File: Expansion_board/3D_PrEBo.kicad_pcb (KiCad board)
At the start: 2 copper layers, 100 x 84 mm, 74 parts, among them J1 LED, J10 TMC_INPUT, J11 Power_out, J12 Z_Probe, J13 Fan_interconnection_header, J14 X_MIN, J15 Z_MAX, J2 V_IN, J3 RJ45, J4 X, J5 Y, J6 Z, J7 E0, J8 E1, J9 FAN&LED_INPUT, M1 Fan_3pin, M2 Fan_3pin, M3 Fan_3pin, M4 Fan_3pin, M5 Fan_3pin, M6 Fan_3pin, M7 Fan_3pin, M8 Fan_4pin, Q1 AOD4189, Q10 IRLML2502, Q2 IRLML2502, Q3 IRLML2502, Q4 IRLML2502, Q5 IRLML2502, Q6 IRLML2502, Q7 IRLML2502, Q8 IRLML2502, Q9 IRLML2502, U1 L5973D, U2 NCP1117-5.0_SOT223

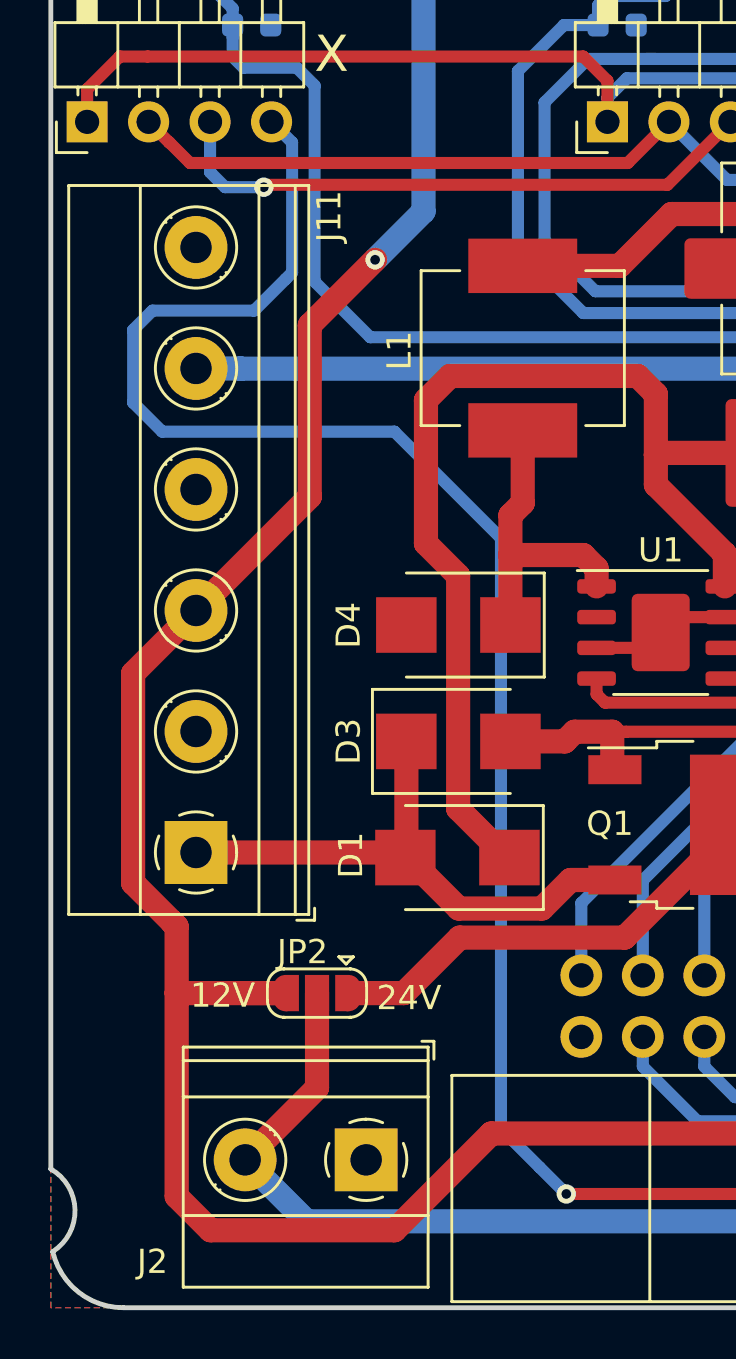
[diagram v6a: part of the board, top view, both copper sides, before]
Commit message: Expansion_board: PCB: Updated silkscreen for power connectors
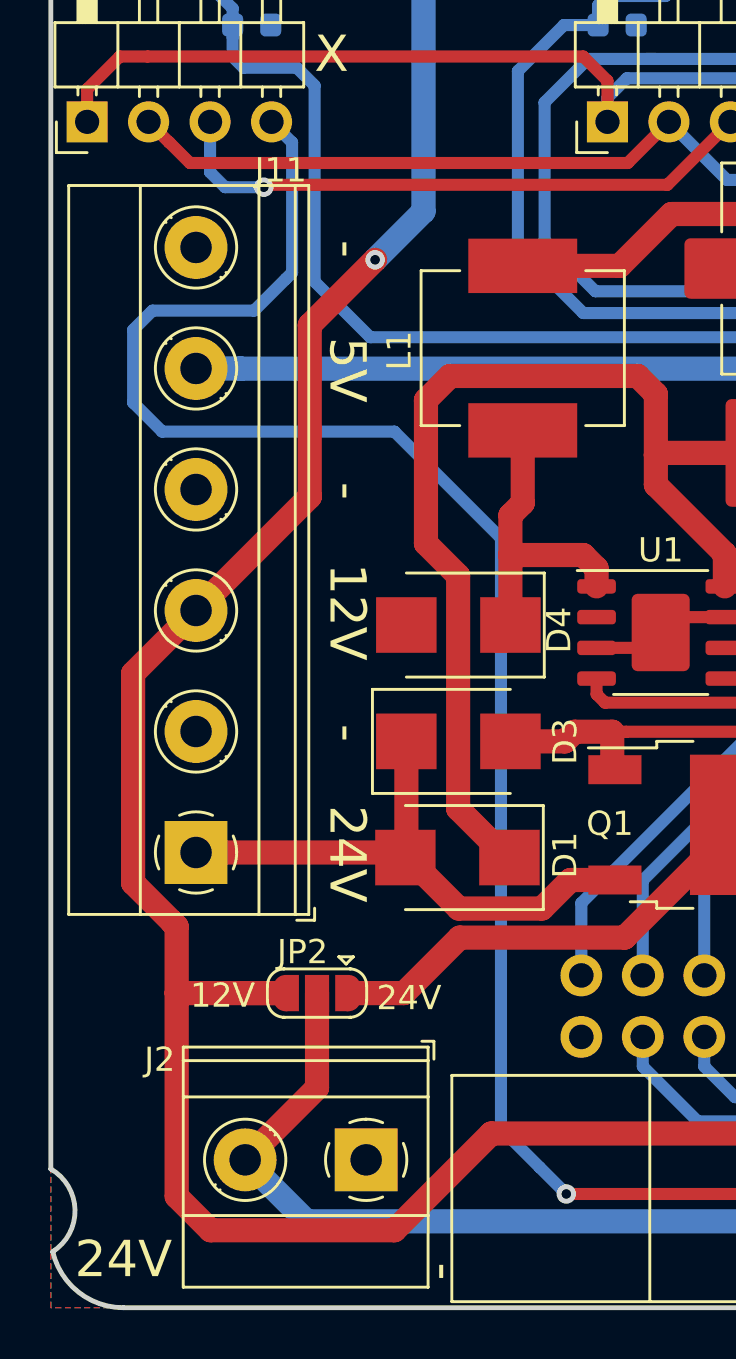
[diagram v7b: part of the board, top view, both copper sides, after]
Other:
- board text added: "-"
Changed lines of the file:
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@@
   (general
     (thickness 1.6)
-    (drawings 173)
+    (drawings 181)
     (tracks 683)
     (zones 0)
@@
     (visible_elements FFFFFFFF)
     (pcbplotparams
-      (layerselection 0x010fc_ffffffff)
-      (usegerberextensions false)
+      (layerselection 0x010f0_ffffffff)
+      (usegerberextensions true)
       (usegerberattributes false)
       (usegerberadvancedattributes false)
       (creategerberjobfile false)
-      (excludeedgelayer true)
+      (excludeedgelayer false)
       (linewidth 0.150000)
       (plotframeref false)
@@
       (outputformat 1)
       (mirror false)
-      (drillshape 1)
+      (drillshape 0)
       (scaleselection 1)
-      (outputdirectory ""))
+      (outputdirectory "gerbers/"))
   )
   (net 0 "")
@@
     (tags "Diode SMB (DO-214AA)")
     (attr smd)
-    (fp_text reference D1 (at 4.4 0.1 270) (layer F.SilkS)
+    (fp_text reference D1 (at -4.45 0.1 270) (layer F.SilkS)
       (effects (font (size 1 1) (thickness 0.15)))
     )
@@
     (tags "Diode SMB (DO-214AA)")
     (attr smd)
-    (fp_text reference D3 (at -4.54 0 90) (layer F.SilkS)
+    (fp_text reference D3 (at 4.41 0 90) (layer F.SilkS)
       (effects (font (size 1 1) (thickness 0.15)))
     )
@@
     (tags "Diode SMB (DO-214AA)")
     (attr smd)
-    (fp_text reference D4 (at 4.54 -0.008 270) (layer F.SilkS)
+    (fp_text reference D4 (at -4.16 -0.208 270) (layer F.SilkS)
       (effects (font (size 1 1) (thickness 0.15)))
     )
@@
     (descr "Terminal Block Phoenix MKDS-1,5-2, 2 pins, pitch 5mm, size 10x9.8mm^2, drill diamater 1.3mm, pad diameter 2.6mm, see http://www.farnell.com/datasheets/100425.pdf, script-generated using https://github.com/pointhi/kicad-footprint-generator/scripts/TerminalBlock_Phoenix")
     (tags "THT Terminal Block Phoenix MKDS-1,5-2 pitch 5mm size 10x9.8mm^2 drill 1.3mm pad 2.6mm")
-    (fp_text reference J2 (at 8.83 -4.21 180) (layer F.SilkS)
+    (fp_text reference J2 (at 8.53 4.14 180) (layer F.SilkS)
       (effects (font (size 1 1) (thickness 0.15)))
     )
@@
     (descr "Terminal Block Phoenix MKDS-1,5-6, 6 pins, pitch 5mm, size 30x9.8mm^2, drill diamater 1.3mm, pad diameter 2.6mm, see http://www.farnell.com/datasheets/100425.pdf, script-generated using https://github.com/pointhi/kicad-footprint-generator/scripts/TerminalBlock_Phoenix")
     (tags "THT Terminal Block Phoenix MKDS-1,5-6 pitch 5mm size 30x9.8mm^2 drill 1.3mm pad 2.6mm")
-    (fp_text reference J11 (at 26.29 5.5 90) (layer F.SilkS)
+    (fp_text reference J11 (at 28.19 3.5 180) (layer F.SilkS)
       (effects (font (size 1 1) (thickness 0.15)))
     )
@@
     )
   )
+  (gr_text 24V (at 103 140) (layer F.SilkS)
+    (effects (font (size 1.5 1.5) (thickness 0.3)))
+  )
+  (gr_text - (at 116 140.5 90) (layer F.SilkS)
+    (effects (font (size 1.5 1.5) (thickness 0.3)))
+  )
+  (gr_text 24V (at 112.25 123.25 270) (layer F.SilkS)
+    (effects (font (size 1.5 1.5) (thickness 0.3)))
+  )
+  (gr_text - (at 112 118.25 90) (layer F.SilkS)
+    (effects (font (size 1.5 1.5) (thickness 0.3)))
+  )
+  (gr_text 12V (at 112.25 113.25 270) (layer F.SilkS)
+    (effects (font (size 1.5 1.5) (thickness 0.3)))
+  )
+  (gr_text - (at 112 108.25 90) (layer F.SilkS)
+    (effects (font (size 1.5 1.5) (thickness 0.3)))
+  )
+  (gr_text 5V (at 112.25 103.25 270) (layer F.SilkS)
+    (effects (font (size 1.5 1.5) (thickness 0.3)))
+  )
+  (gr_text - (at 112 98.25 90) (layer F.SilkS)
+    (effects (font (size 1.5 1.5) (thickness 0.3)))
+  )
   (gr_text MI (at 180.5 116.95) (layer F.SilkS)

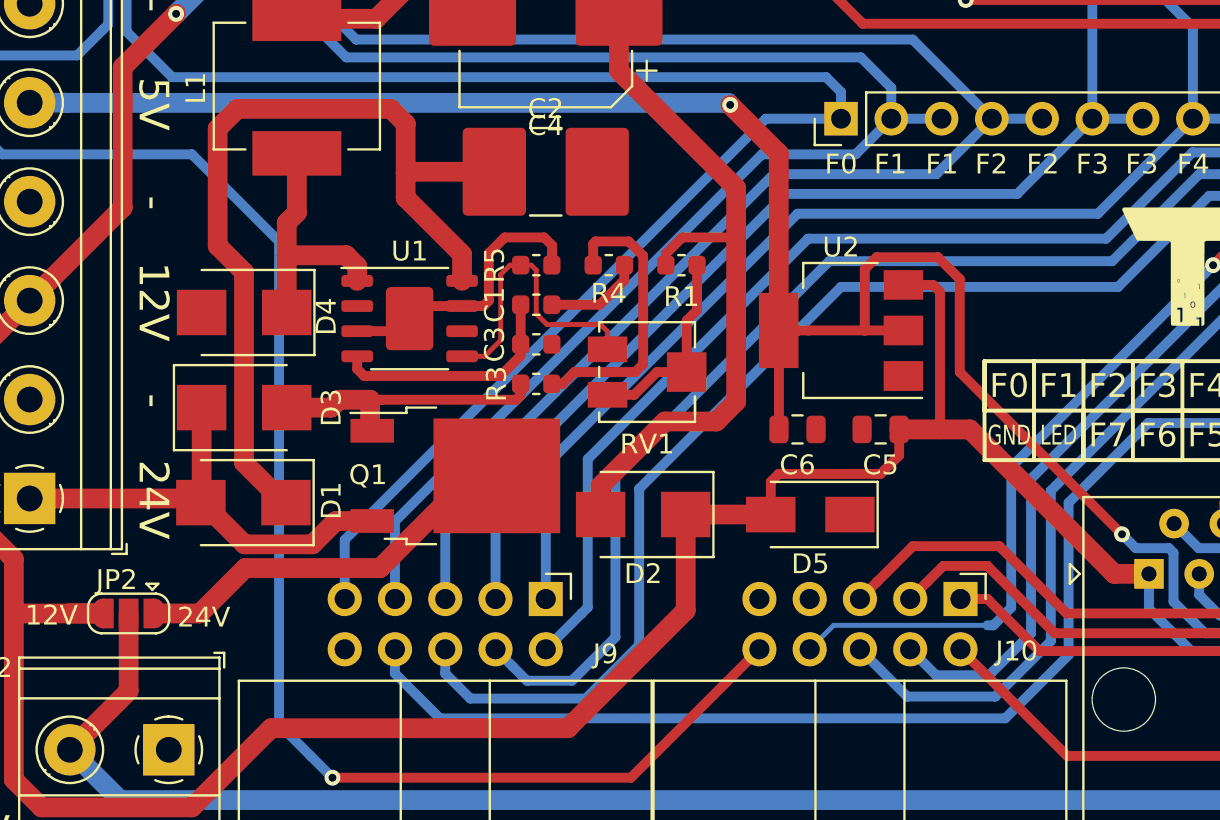
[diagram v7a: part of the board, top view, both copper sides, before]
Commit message: Expansion_board: Add test points for voltages
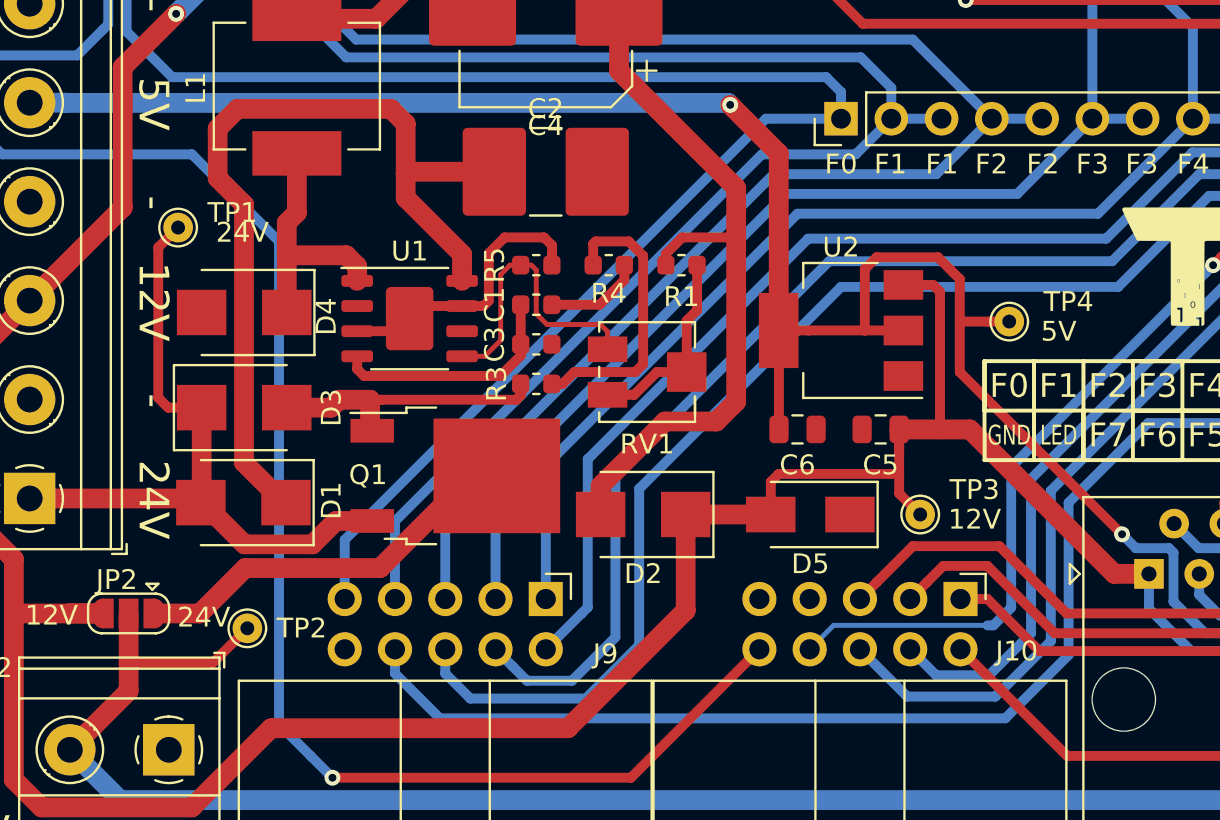
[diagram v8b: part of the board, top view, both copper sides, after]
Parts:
- added TP1: 24V, TestPoint:TestPoint_THTPad_D1.5mm_Drill0.7mm, F.Cu at (113.5, 109.5)
- added TP2: V_IN, TestPoint:TestPoint_THTPad_D1.5mm_Drill0.7mm, F.Cu at (117.0, 129.8)
- added TP3: 12V, TestPoint:TestPoint_THTPad_D1.5mm_Drill0.7mm, F.Cu at (151.0, 124.0)
- added TP4: 5V, TestPoint:TestPoint_THTPad_D1.5mm_Drill0.7mm, F.Cu at (155.5, 114.2)
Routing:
- net +24V: track 23.6 -> 35.0 mm
- net V_IN: track 79.7 -> 86.4 mm
- net +12V: track 317.7 -> 322.1 mm
- net +5V: track 113.5 -> 116.0 mm
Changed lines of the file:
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@@
   (general
     (thickness 1.6)
-    (drawings 181)
-    (tracks 683)
+    (drawings 184)
+    (tracks 696)
     (zones 0)
-    (modules 74)
+    (modules 78)
     (nets 59)
   )
@@
   )
   (setup
-    (last_trace_width 0.25)
+    (last_trace_width 0.5)
     (user_trace_width 0.5)
     (user_trace_width 1)
@@
     )
   )
+  (module TestPoint:TestPoint_THTPad_D1.5mm_Drill0.7mm (layer F.Cu)
+    (at 113.5 109.5)
+    (descr "THT pad as test Point, diameter 1.5mm, hole diameter 0.7mm")
+    (tags "test point THT pad")
+    (attr virtual)
+    (fp_text reference TP1 (at 2.75 -0.75) (layer F.SilkS)
+      (effects (font (size 1 1) (thickness 0.15)))
+    )
+    (fp_text value 24V (at 0 1.75) (layer F.Fab)
+      (effects (font (size 1 1) (thickness 0.15)))
+    )
+    (fp_circle (center 0 0) (end 0 0.95) (layer F.SilkS) (width 0.12))
+    (fp_circle (center 0 0) (end 1.25 0) (layer F.CrtYd) (width 0.05))
+    (fp_text user %R (at 0 -1.65) (layer F.Fab)
+      (effects (font (size 1 1) (thickness 0.15)))
+    )
+    (pad 1 thru_hole circle (at 0 0) (size 1.5 1.5) (drill 0.7) (layers *.Cu *.Mask)
+      (net 15 +24V))
+  )
+  (module TestPoint:TestPoint_THTPad_D1.5mm_Drill0.7mm (layer F.Cu)
+    (at 117 129.75)
+    (descr "THT pad as test Point, diameter 1.5mm, hole diameter 0.7mm")
+    (tags "test point THT pad")
+    (attr virtual)
+    (fp_text reference TP2 (at 2.75 0) (layer F.SilkS)
+      (effects (font (size 1 1) (thickness 0.15)))
+    )
+    (fp_text value V_IN (at 0 1.75) (layer F.Fab)
+      (effects (font (size 1 1) (thickness 0.15)))
+    )
+    (fp_text user %R (at 0 -1.65) (layer F.Fab)
+      (effects (font (size 1 1) (thickness 0.15)))
+    )
+    (fp_circle (center 0 0) (end 1.25 0) (layer F.CrtYd) (width 0.05))
+    (fp_circle (center 0 0) (end 0 0.95) (layer F.SilkS) (width 0.12))
+    (pad 1 thru_hole circle (at 0 0) (size 1.5 1.5) (drill 0.7) (layers *.Cu *.Mask)
+      (net 58 V_IN))
+  )
+  (module TestPoint:TestPoint_THTPad_D1.5mm_Drill0.7mm (layer F.Cu)
+    (at 151 124)
+    (descr "THT pad as test Point, diameter 1.5mm, hole diameter 0.7mm")
+    (tags "test point THT pad")
+    (attr virtual)
+    (fp_text reference TP3 (at 2.75 -1.25) (layer F.SilkS)
+      (effects (font (size 1 1) (thickness 0.15)))
+    )
+    (fp_text value 12V (at 0 1.75) (layer F.Fab)
+      (effects (font (size 1 1) (thickness 0.15)))
+    )
+    (fp_text user %R (at 0 -1.65) (layer F.Fab)
+      (effects (font (size 1 1) (thickness 0.15)))
+    )
+    (fp_circle (center 0 0) (end 1.25 0) (layer F.CrtYd) (width 0.05))
+    (fp_circle (center 0 0) (end 0 0.95) (layer F.SilkS) (width 0.12))
+    (pad 1 thru_hole circle (at 0 0) (size 1.5 1.5) (drill 0.7) (layers *.Cu *.Mask)
+      (net 6 +12V))
+  )
+  (module TestPoint:TestPoint_THTPad_D1.5mm_Drill0.7mm (layer F.Cu)
+    (at 155.5 114.25)
+    (descr "THT pad as test Point, diameter 1.5mm, hole diameter 0.7mm")
+    (tags "test point THT pad")
+    (attr virtual)
+    (fp_text reference TP4 (at 3 -1) (layer F.SilkS)
+      (effects (font (size 1 1) (thickness 0.15)))
+    )
+    (fp_text value 5V (at 0 1.75) (layer F.Fab)
+      (effects (font (size 1 1) (thickness 0.15)))
+    )
+    (fp_circle (center 0 0) (end 0 0.95) (layer F.SilkS) (width 0.12))
+    (fp_circle (center 0 0) (end 1.25 0) (layer F.CrtYd) (width 0.05))
+    (fp_text user %R (at 0 -1.65) (layer F.Fab)
+      (effects (font (size 1 1) (thickness 0.15)))
+    )
+    (pad 1 thru_hole circle (at 0 0) (size 1.5 1.5) (drill 0.7) (layers *.Cu *.Mask)
+      (net 7 +5V))
+  )
+  (gr_text 24V (at 116.75 109.75) (layer F.SilkS)
+    (effects (font (size 1 1) (thickness 0.2)))
+  )
+  (gr_text 12V (at 153.75 124.25) (layer F.SilkS)
+    (effects (font (size 1 1) (thickness 0.2)))
+  )
+  (gr_text 5V (at 158 114.75) (layer F.SilkS)
+    (effects (font (size 1 1) (thickness 0.2)))
+  )
   (gr_text 24V (at 103 140) (layer F.SilkS)
     (effects (font (size 1.5 1.5) (thickness 0.3)))
@@
   (segment (start 125 104.25) (end 125 106.75) (width 1) (layer F.Cu) (net 4))
   (segment (start 124.25 103.5) (end 125 104.25) (width 1) (layer F.Cu) (net 4))
+  (segment (start 116.5 103.5) (end 124.25 103.5) (width 1) (layer F.Cu) (net 4))
   (segment (start 118.95 123.4) (end 118.85 123.4) (width 1) (layer F.Cu) (net 4))
+  (segment (start 116.83 121.38) (end 116.83 108.33) (width 1) (layer F.Cu) (net 4))
+  (segment (start 116.83 108.33) (end 115.5 107) (width 1) (layer F.Cu) (net 4))
   (segment (start 118.85 123.4) (end 116.83 121.38) (width 1) (layer F.Cu) (net 4))
-  (segment (start 116.83 121.38) (end 116.83 111.75) (width 1) (layer F.Cu) (net 4))
-  (segment (start 116.83 111.75) (end 115.5 110.42) (width 1) (layer F.Cu) (net 4))
-  (segment (start 115.5 110.42) (end 115.5 104.5) (width 1) (layer F.Cu) (net 4))
-  (segment (start 116.5 103.5) (end 124.25 103.5) (width 1) (layer F.Cu) (net 4))
+  (segment (start 115.5 107) (end 115.5 104.5) (width 1) (layer F.Cu) (net 4))
   (segment (start 115.5 104.5) (end 116.5 103.5) (width 1) (layer F.Cu) (net 4))
   (segment (start 134.85 122.55) (end 134.85 124) (width 1) (layer F.Cu) (net 5))
@@
   (segment (start 139.35 124.2) (end 139.15 124) (width 1) (layer F.Cu) (net 6))
   (segment (start 143.45 124) (end 139.15 124) (width 1) (layer F.Cu) (net 6))
-  (segment (start 143.85 121.95) (end 143.45 122.35) (width 0.5) (layer F.Cu) (net 6))
-  (segment (start 149 121.95) (end 143.85 121.95) (width 0.5) (layer F.Cu) (net 6))
   (segment (start 149.9375 119.7) (end 149.9375 121.0125) (width 0.5) (layer F.Cu) (net 6))
-  (segment (start 143.45 122.35) (end 143.45 124) (width 0.5) (layer F.Cu) (net 6))
-  (segment (start 149.9375 121.0125) (end 149 121.95) (width 0.5) (layer F.Cu) (net 6))
+  (segment (start 149.9375 122.9375) (end 151 124) (width 0.5) (layer F.Cu) (net 6))
+  (segment (start 149.8875 121.95) (end 149.9375 122) (width 0.5) (layer F.Cu) (net 6))
+  (segment (start 143.45 122.35) (end 143.85 121.95) (width 0.5) (layer F.Cu) (net 6))
+  (segment (start 143.45 124) (end 143.45 122.35) (width 0.5) (layer F.Cu) (net 6))
+  (segment (start 149.9375 119.7) (end 149.9375 122) (width 0.5) (layer F.Cu) (net 6))
+  (segment (start 143.85 121.95) (end 149.8875 121.95) (width 0.5) (layer F.Cu) (net 6))
+  (segment (start 149.9375 122) (end 149.9375 122.9375) (width 0.5) (layer F.Cu) (net 6))
   (segment (start 143.8625 114.7125) (end 143.85 114.7) (width 0.5) (layer F.Cu) (net 7))
   (segment (start 143.8625 119.7) (end 143.8625 114.7125) (width 0.5) (layer F.Cu) (net 7))
@@
   (segment (start 148.2 114.7) (end 148.2 111.6) (width 0.5) (layer F.Cu) (net 7))
   (segment (start 153 116.8) (end 161.2 125) (width 0.5) (layer F.Cu) (net 7))
-  (segment (start 153 112.1) (end 153 116.8) (width 0.5) (layer F.Cu) (net 7))
   (segment (start 148.2 111.6) (end 148.8 111) (width 0.5) (layer F.Cu) (net 7))
   (segment (start 178.7 134) (end 185.405 134) (width 0.5) (layer B.Cu) (net 7))
@@
   (segment (start 163.8 125.929998) (end 163.8 128.4) (width 0.5) (layer B.Cu) (net 7))
   (segment (start 165.4 130) (end 174.7 130) (width 0.5) (layer B.Cu) (net 7))
+  (segment (start 155.5 114.25) (end 154.43934 114.25) (width 0.5) (layer F.Cu) (net 7))
+  (segment (start 154.43934 114.25) (end 153 114.25) (width 0.5) (layer F.Cu) (net 7))
+  (segment (start 153 112.1) (end 153 114.25) (width 0.5) (layer F.Cu) (net 7))
+  (segment (start 153 114.25) (end 153 116.8) (width 0.5) (layer F.Cu) (net 7))
   (segment (start 110.225 67.655) (end 109.3 68.58) (width 0.5) (layer B.Cu) (net 8))
   (segment (start 110.225 66) (end 110.225 67.655) (width 0.5) (layer B.Cu) (net 8))
@@
   (segment (start 116.856388 125.506388) (end 120.293612 125.506388) (width 1) (layer F.Cu) (net 15))
   (segment (start 114.65 123.4) (end 114.75 123.4) (width 1) (layer F.Cu) (net 15))
+  (segment (start 112.5 118.1) (end 112.5 110.5) (width 0.5) (layer F.Cu) (net 15))
+  (segment (start 114.69 118.6) (end 113 118.6) (width 0.5) (layer F.Cu) (net 15))
+  (segment (start 113 118.6) (end 112.5 118.1) (width 0.5) (layer F.Cu) (net 15))
+  (segment (start 112.5 110.5) (end 113.5 109.5) (width 0.5) (layer F.Cu) (net 15))
   (segment (start 118.99 118.364) (end 118.89 118.364) (width 1) (layer F.Cu) (net 16))
   (segment (start 130.5875 118.2) (end 123.775 118.2) (width 0.5) (layer F.Cu) (net 16))
@@
   (segment (start 129.8 115.2) (end 128.995 116.005) (width 0.25) (layer F.Cu) (net 55))
   (segment (start 130.275 111.4) (end 129.8 111.875) (width 0.25) (layer F.Cu) (net 55))
-  (segment (start 111 132.92) (end 111 129) (width 1) (layer F.Cu) (net 58))
   (segment (start 108.03 135.89) (end 111 132.92) (width 1) (layer F.Cu) (net 58))
   (segment (start 110.57 138.43) (end 178.555 138.43) (width 1) (layer B.Cu) (net 58))
   (segment (start 108.03 135.89) (end 110.57 138.43) (width 1) (layer B.Cu) (net 58))
+  (segment (start 115.25 131.5) (end 117 129.75) (width 0.5) (layer F.Cu) (net 58))
+  (segment (start 111 131.5) (end 115.25 131.5) (width 0.5) (layer F.Cu) (net 58))
+  (segment (start 111 132.92) (end 111 131.5) (width 1) (layer F.Cu) (net 58))
+  (segment (start 111 131.5) (end 111 129) (width 1) (layer F.Cu) (net 58))
   (zone (net 3) (net_name GND) (layer F.Cu) (hatch edge 0.508)
     (connect_pads (clearance 0.508))
